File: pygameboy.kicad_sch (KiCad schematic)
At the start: 142 parts, among them J1 Conn_01x01, J2 Conn_01x01, J3 Conn_ARM_JTAG_SWD_10, J4 USB_B_Micro, J5 MIDI IN, J6 MIDI OUT, Q1 BSS138, SW1 SW_Push, U1 CARTRIDGE, U2 RP2040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

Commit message: More work on RP2350B
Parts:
- removed C1, C2: 22pF, Capacitor_SMD:C_0402_1005Metric_Pad0.74x0.62mm_HandSolder, symbol Device:C_Small
- removed C11, C12, C14, C15, C18, C20, C21, C22, C3, C5, C6, C9: 0.1uF, Capacitor_SMD:C_0603_1608Metric_Pad1.08x0.95mm_HandSolder, symbol Device:C_Small
- removed C19, C4: 1uF, Capacitor_SMD:C_0603_1608Metric_Pad1.08x0.95mm_HandSolder, symbol Device:C_Small
- removed J4: USB_B_Micro, adafruit:4UCONN_20329_V2_USB, symbol Connector:USB_B_Micro
- removed R10: 1k, Resistor_SMD:R_0603_1608Metric_Pad0.98x0.95mm_HandSolder, symbol Device:R_Small
- removed R11, R12: 27, Resistor_SMD:R_0603_1608Metric_Pad0.98x0.95mm_HandSolder, symbol Device:R_Small
- removed R9: 10k, Resistor_SMD:R_0603_1608Metric_Pad0.98x0.95mm_HandSolder, symbol Device:R_Small
- removed TP33: Test_Point, keystone:5015-SMT-TestPoint, symbol Connector:TestPoint
- removed TP34: DATA_OE, keystone:5015-SMT-TestPoint, symbol Connector:TestPoint
- removed TP35: GB_RESET, keystone:5015-SMT-TestPoint, symbol Connector:TestPoint
- removed TP37: gnd, keystone:5015-SMT-TestPoint, symbol Connector:TestPoint
- removed TP38: 3.3v, keystone:5015-SMT-TestPoint, symbol Connector:TestPoint
- removed TP39: batt, keystone:5015-SMT-TestPoint, symbol Connector:TestPoint
- removed TP40: clk, keystone:5015-SMT-TestPoint, symbol Connector:TestPoint
- removed TP41: rd, keystone:5015-SMT-TestPoint, symbol Connector:TestPoint
- removed TP42: wr, keystone:5015-SMT-TestPoint, symbol Connector:TestPoint
- removed TP43: a15, keystone:5015-SMT-TestPoint, symbol Connector:TestPoint
- removed TP45: cs, keystone:5015-SMT-TestPoint, symbol Connector:TestPoint
- removed TP46: data0, keystone:5015-SMT-TestPoint, symbol Connector:TestPoint
- removed TP47: D0, keystone:5015-SMT-TestPoint, symbol Connector:TestPoint
- removed TP80, TP81, TP82, TP83, TP84, TP85: Test_Point, TestPoint:TestPoint_Pad_D1.5mm, symbol Connector:TestPoint
- removed U2: RP2040, MCU_RaspberryPi_and_Boards:RP2040-QFN-56, symbol MCU_RaspberryPi_and_Boards:RP2040
- removed U3, U4, U6: 74LVC244, Package_SO:TSSOP-20_4.4x6.5mm_P0.65mm, symbol 74xx:74HC244
- removed U9: W25Q32JVSS, Package_SO:SOIC-8_5.23x5.23mm_P1.27mm, symbol pygameboy-rescue:W25Q32JVSS-Memory_Flash
- removed Y1: 12mhz, Crystal:Crystal_SMD_Abracon_ABM3C-4Pin_5.0x3.2mm, symbol Device:Crystal
- added J4: USB_C_Receptacle_USB2.0_16P, Adafruit:USB_C_Receptacle_HRO_TYPE-C-31-M-31, symbol Connector:USB_C_Receptacle_USB2.0_16P
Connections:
- net GND: now also J4.A1 (GND), J4.A12 (GND), J4.B1 (GND), J4.B12 (GND), J4.SH (SHIELD)
- net USB_D+: now also J4.A6 (D+), J4.B6 (D+)
- net USB_D-: now also J4.A7 (D-), J4.B7 (D-)
- net VBUS: now also J4.A4 (VBUS), J4.A9 (VBUS), J4.B4 (VBUS), J4.B9 (VBUS)
- no-connect marks 12 -> 9
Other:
- added sheet RP2350 Core (rp2350.kicad_sch)
- moved on the sheet: C16, R1, SW1, TP36

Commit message: Ordered!
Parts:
- removed J3: Conn_ARM_JTAG_SWD_10, Pin_Headers:Pin_Header_Straight_2x05_Pitch1.27mm_SMD, symbol pygameboy-rescue:Conn_ARM_JTAG_SWD_10-Connector
- removed J5: MIDI IN, adafruit:4UCONN_19269_TRS, symbol pygameboy-rescue:AudioJack3_SwitchTR-Connector
- removed J6: MIDI OUT, adafruit:4UCONN_19269_TRS, symbol pygameboy-rescue:AudioJack3_SwitchTR-Connector
- removed TP36: SAMD_RESET, keystone:5015-SMT-TestPoint, symbol Connector:TestPoint
- added C2: 47uF, Capacitor_SMD:C_0805_2012Metric, symbol Device:C_Small
- added J14: Conn_01x04, Connector_JST:JST_SH_SM04B-SRSS-TB_1x04-1MP_P1.00mm_Horizontal, symbol Connector_Generic:Conn_01x04
- added J5, J6: AudioJack4, Connector_Audio:Jack_3.5mm_PJ320D_Horizontal, symbol Connector_Audio:AudioJack4
- added R10, R9: 5.1k, Resistor_SMD:R_0402_1005Metric, symbol Device:R_Small
- added R11: 10k, Resistor_SMD:R_0402_1005Metric, symbol Device:R_Small
- added SW2: SW_Push, Button_Switch_SMD:SW_SPST_TS-1088-xR020, symbol Switch:SW_Push
- C10, C13: footprint Capacitor_SMD:C_0603_1608Metric_Pad1.08x0.95mm_HandSolder -> Capacitor_SMD:C_0402_1005Metric
- C16, C17: value C_Small -> 100n; footprint Capacitor_SMD:C_0603_1608Metric_Pad1.08x0.95mm_HandSolder -> Capacitor_SMD:C_0402_1005Metric
- C7, C8: value 0.1uF -> 100n; footprint Capacitor_SMD:C_0603_1608Metric_Pad1.08x0.95mm_HandSolder -> Capacitor_SMD:C_0402_1005Metric
- D3: footprint LED_SMD:LED_0805_2012Metric_Pad1.15x1.40mm_HandSolder -> LED_SMD:LED_0603_1608Metric
- Q1: footprint TO_SOT_Packages_SMD:SOT-23 -> Package_TO_SOT_SMD:SOT-23
- R1, R2, R3, R5, R6, R7, R8: footprint Resistor_SMD:R_0603_1608Metric_Pad0.98x0.95mm_HandSolder -> Resistor_SMD:R_0402_1005Metric
- R4: value 1k -> 5.1k; footprint Resistor_SMD:R_0603_1608Metric_Pad0.98x0.95mm_HandSolder -> Resistor_SMD:R_0402_1005Metric
- SW1: footprint Button_Switch_SMD:SW_SPST_KMR2 -> Button_Switch_SMD:SW_SPST_TS-1088-xR020
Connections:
- net 3V_RD is gone; now on net RD: U5.2 (DIR)
- net SAMD_RESET is gone; now on net RESET: C16.1, R1.2, SW1.1
- net +3V3: now also J14.2 (Pin_2)
- net AUD: now also C2.2, R11.1
- net GB_RESET: now also Q1.3 (D), TP30.1, TP77.1, U1.30 (RESET); no longer Q1.1 (G), R2.2
- net GND: now also J14.1 (Pin_1), J6.S, R10.1, R11.2, R9.1, SW2.2
- net RESET: no longer Q1.3 (D), TP30.1, TP77.1, U1.30 (RESET)
- net SHIELD: now also J5.S
- net at D4.2 (A), U8.2: now also J5.R1, J5.R2
- net at R5.2: now also J5.T
- net at R7.2: now also J6.R1, J6.R2
- net at R6.2: now also J6.T
- net at J4.A5 (CC1): now also R9.2
- net at J4.B5 (CC2): now also R10.2
- new net BOOT: SW2.1
- new net PWM_AUDIO: C2.1
- new net RP_GB_RESET: Q1.1 (G), R2.2
- new net SCL: J14.4 (Pin_4)
- new net SDA: J14.3 (Pin_3)
- no-connect marks 9 -> 4
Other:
- sheet RP2350 Core ports: added QSPI_SS, RUN, USB_D+, USB_D-; removed none
- moved on the sheet: R5

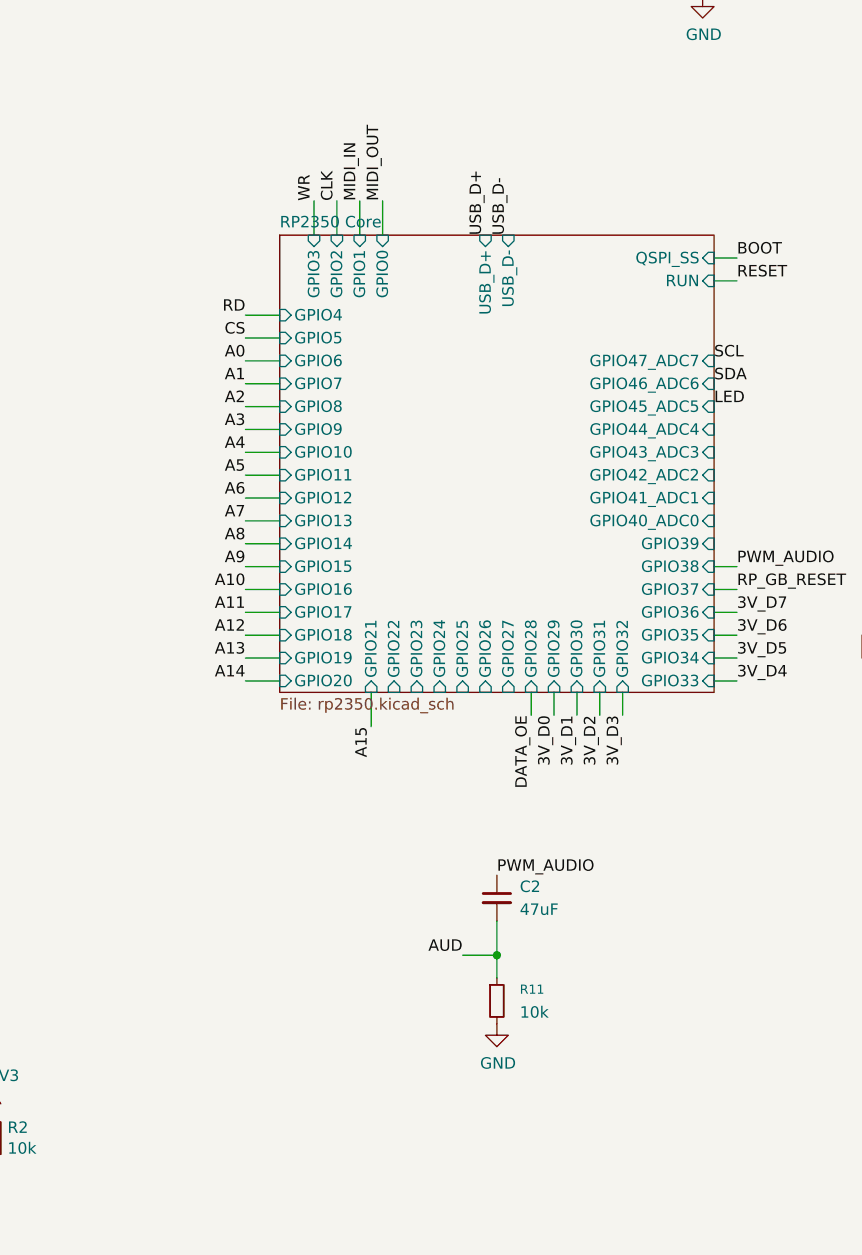
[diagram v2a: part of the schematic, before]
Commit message: Fix reset circuit. Move control signals to higher pins that both PIO offsets can read. Redo audio circuit
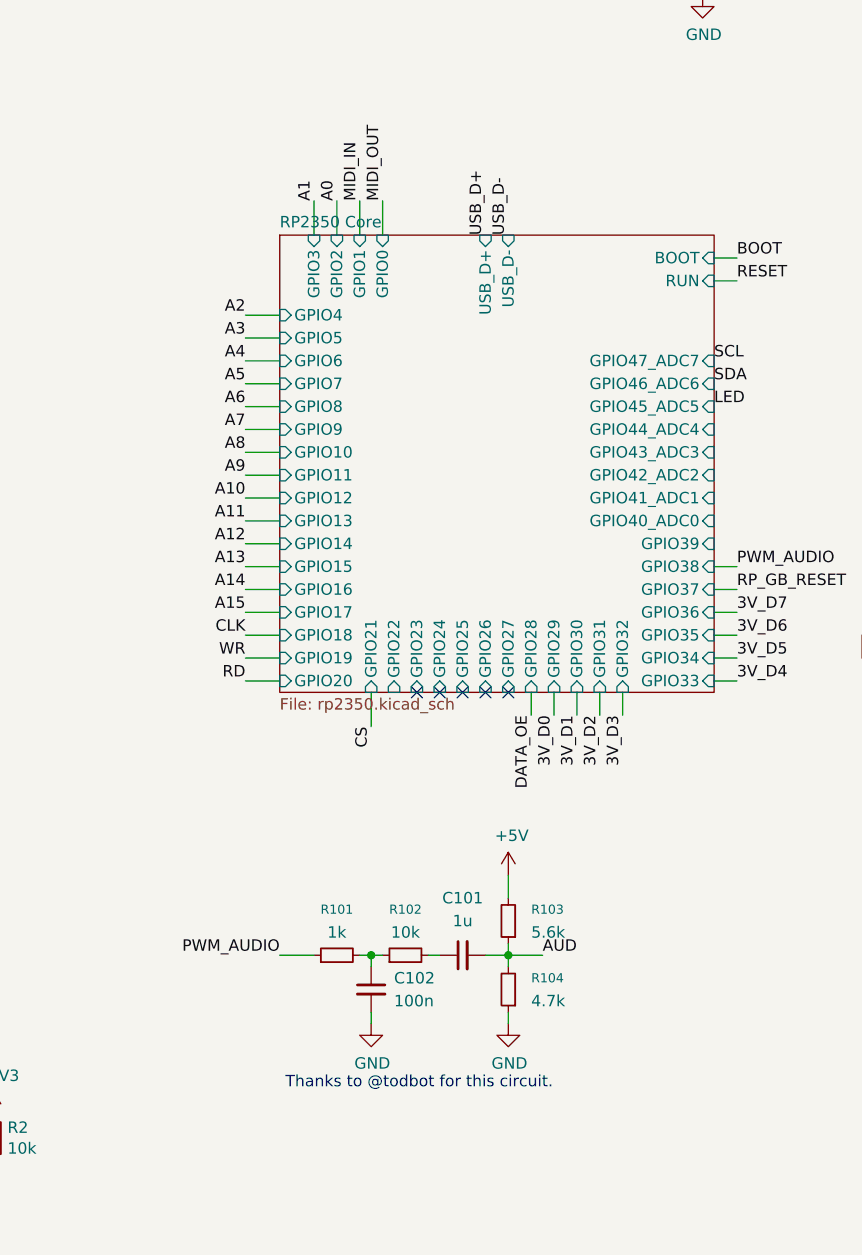
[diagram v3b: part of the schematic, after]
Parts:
- added C101: 1u, Capacitor_SMD:C_0603_1608Metric_Pad1.08x0.95mm_HandSolder, symbol Device:C_Small
- added R101: 1k, Resistor_SMD:R_0603_1608Metric_Pad0.98x0.95mm_HandSolder, symbol Device:R_Small
- added R103: 5.6k, Resistor_SMD:R_0603_1608Metric_Pad0.98x0.95mm_HandSolder, symbol Device:R_Small
- added R104: 4.7k, Resistor_SMD:R_0603_1608Metric_Pad0.98x0.95mm_HandSolder, symbol Device:R_Small
- C102: renamed from C2; value 47uF -> 100n; footprint Capacitor_SMD:C_0805_2012Metric -> Capacitor_SMD:C_0603_1608Metric_Pad1.08x0.95mm_HandSolder
- R102: renamed from R11; footprint Resistor_SMD:R_0402_1005Metric -> Resistor_SMD:R_0603_1608Metric_Pad0.98x0.95mm_HandSolder
- R6, R7: footprint Resistor_SMD:R_0402_1005Metric -> Resistor_SMD:R_0603_1608Metric
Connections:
- net +5V: now also R103.2
- net AUD: now also C101.2, R103.1, R104.2; no longer C102.2, R102.1
- net GND: now also C102.2, R104.1; no longer R102.2
- net PWM_AUDIO: now also R101.1; no longer C102.1
- new net: C101.1, R102.2
- new net: C102.1, R101.2, R102.1
- no-connect marks 4 -> 9
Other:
- sheet RP2350 Core ports: added BOOT; removed QSPI_SS
- note added: "Thanks to @todbot for this circuit."
- moved on the sheet: C102, R102
